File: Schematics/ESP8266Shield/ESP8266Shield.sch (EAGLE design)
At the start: 23 parts, among them IC1 MEGA8-P, Q1 2N5088, Q2 2N5088

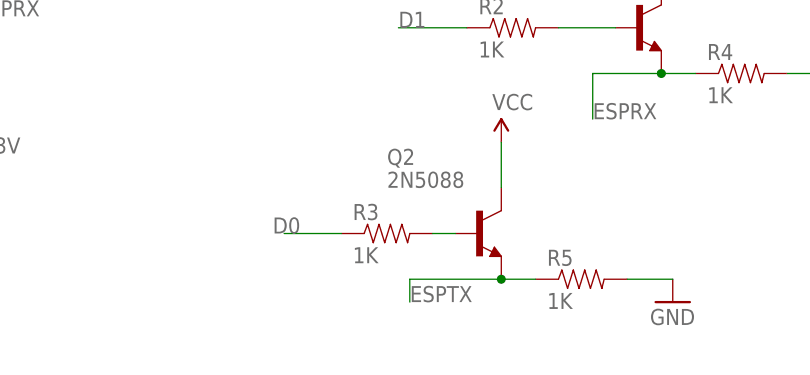
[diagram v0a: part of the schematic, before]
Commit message: v0.08
Updated Android project to close socket on exit
Updated Arduino projects
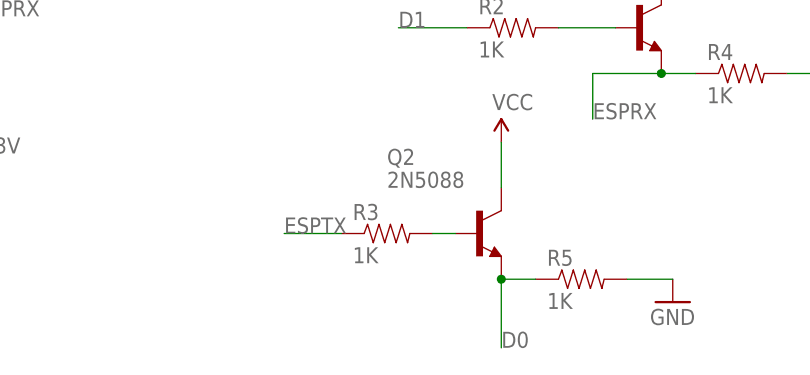
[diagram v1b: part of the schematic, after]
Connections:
- net D0: now also Q2.E, R5.1; no longer R3.1
- net ESPTX: now also R3.1; no longer Q2.E, R5.1
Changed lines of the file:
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@@
-</segment>
-<segment>
-<pinref part="R3" gate="G$1" pin="1"/>
-<wire x1="121.92" y1="-29.21" x2="115.57" y2="-29.21" width="0.1524" layer="91"/>
-<label x="114.3" y="-29.21" size="1.778" layer="95"/>
 </segment>
 <segment>
@@
 <junction x="172.72" y="55.88"/>
 <wire x1="172.72" y1="55.88" x2="175.26" y2="55.88" width="0.1524" layer="91"/>
+</segment>
+<segment>
+<pinref part="Q2" gate="G$1" pin="E"/>
+<pinref part="R5" gate="G$1" pin="1"/>
+<wire x1="143.51" y1="-34.29" x2="139.7" y2="-34.29" width="0.1524" layer="91"/>
+<wire x1="139.7" y1="-34.29" x2="139.7" y2="-41.91" width="0.1524" layer="91"/>
+<junction x="139.7" y="-34.29"/>
+<label x="139.7" y="-41.91" size="1.778" layer="95"/>
 </segment>
 </net>
@@
 </segment>
 <segment>
-<pinref part="Q2" gate="G$1" pin="E"/>
-<pinref part="R5" gate="G$1" pin="1"/>
-<wire x1="143.51" y1="-34.29" x2="139.7" y2="-34.29" width="0.1524" layer="91"/>
-<wire x1="139.7" y1="-34.29" x2="129.54" y2="-34.29" width="0.1524" layer="91"/>
-<wire x1="129.54" y1="-34.29" x2="129.54" y2="-36.83" width="0.1524" layer="91"/>
-<junction x="139.7" y="-34.29"/>
-<label x="129.54" y="-36.83" size="1.778" layer="95"/>
+<pinref part="R3" gate="G$1" pin="1"/>
+<wire x1="121.92" y1="-29.21" x2="115.57" y2="-29.21" width="0.1524" layer="91"/>
+<label x="115.57" y="-29.21" size="1.778" layer="95"/>
 </segment>
 </net>

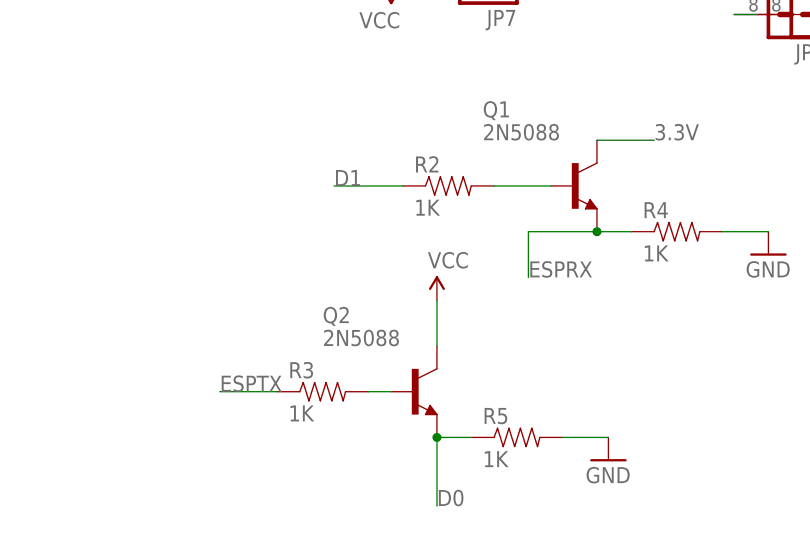
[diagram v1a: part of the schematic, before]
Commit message: V0.13
Updated ESP8266_Shield so that soft-serial can be used.
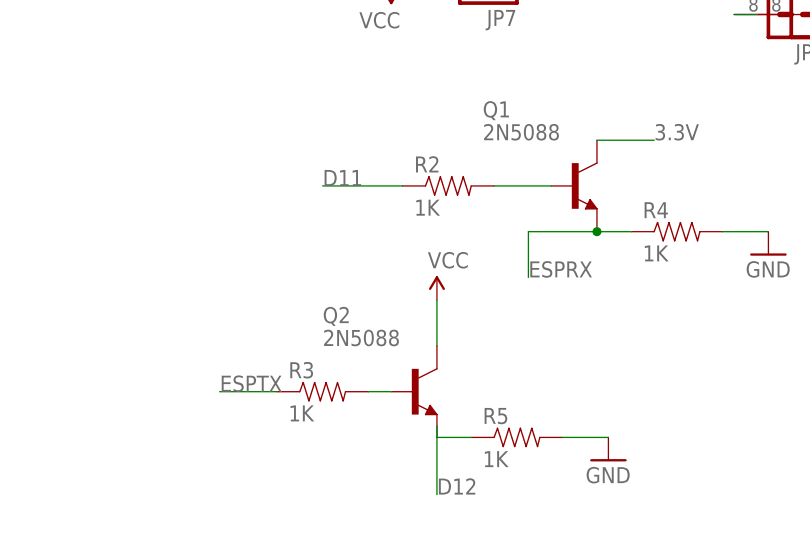
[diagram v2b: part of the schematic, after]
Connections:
- net D1: no longer R2.1
- net D11: now also R2.1
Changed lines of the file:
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@@
 <wire x1="172.72" y1="20.32" x2="175.26" y2="20.32" width="0.1524" layer="91"/>
+</segment>
+<segment>
+<wire x1="139.7" y1="-33.02" x2="139.7" y2="-40.64" width="0.1524" layer="91"/>
+<label x="139.7" y="-40.64" size="1.778" layer="95"/>
 </segment>
 </net>
@@
 <wire x1="172.72" y1="22.86" x2="175.26" y2="22.86" width="0.1524" layer="91"/>
 </segment>
+<segment>
+<pinref part="R2" gate="G$1" pin="1"/>
+<wire x1="135.89" y1="-6.35" x2="127" y2="-6.35" width="0.1524" layer="91"/>
+<label x="127" y="-6.35" size="1.778" layer="95"/>
+</segment>
 </net>
 <net name="D13" class="0">
@@
 </segment>
 <segment>
-<pinref part="R2" gate="G$1" pin="1"/>
-<wire x1="135.89" y1="-6.35" x2="128.27" y2="-6.35" width="0.1524" layer="91"/>
-<label x="128.27" y="-6.35" size="1.778" layer="95"/>
-</segment>
-<segment>
 <pinref part="JP3" gate="G$1" pin="2"/>
 <wire x1="172.72" y1="53.34" x2="163.83" y2="53.34" width="0.1524" layer="91"/>
@@
 <pinref part="R5" gate="G$1" pin="1"/>
 <wire x1="143.51" y1="-34.29" x2="139.7" y2="-34.29" width="0.1524" layer="91"/>
-<wire x1="139.7" y1="-34.29" x2="139.7" y2="-41.91" width="0.1524" layer="91"/>
-<junction x="139.7" y="-34.29"/>
-<label x="139.7" y="-41.91" size="1.778" layer="95"/>
-</segment>
-</net>
+</segment>
+</net>
